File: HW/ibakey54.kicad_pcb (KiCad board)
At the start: 4 copper layers, 164.1 x 143 mm, 106 parts, among them SW1 GATERON-MX-HOTSWAP-RGB, SW10 GATERON-MX-HOTSWAP-RGB, SW11 GATERON-MX-HOTSWAP-RGB, SW12 GATERON-MX-HOTSWAP-RGB, SW13 GATERON-MX-HOTSWAP-RGB, SW14 GATERON-MX-HOTSWAP-RGB, SW15 GATERON-MX-HOTSWAP-RGB, SW16 GATERON-MX-HOTSWAP-RGB, SW17 GATERON-MX-HOTSWAP-RGB, SW18 GATERON-MX-HOTSWAP-RGB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

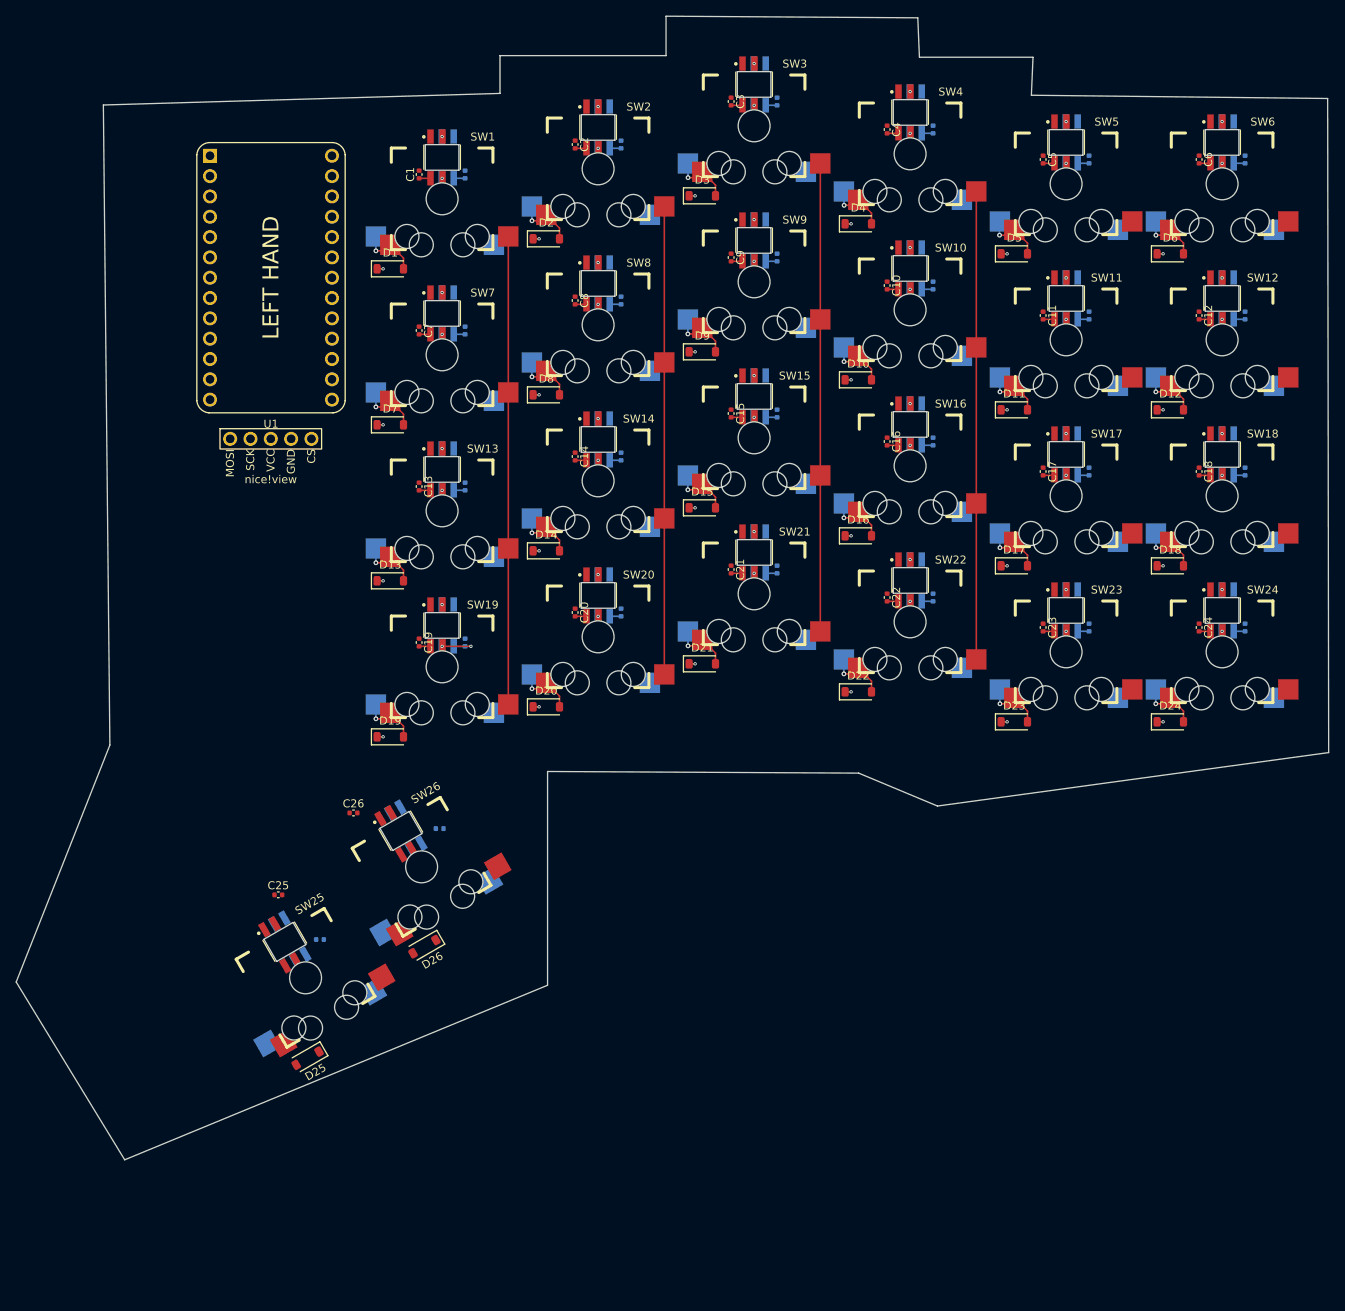
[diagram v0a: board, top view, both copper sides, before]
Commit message: finishing main placement & board shape
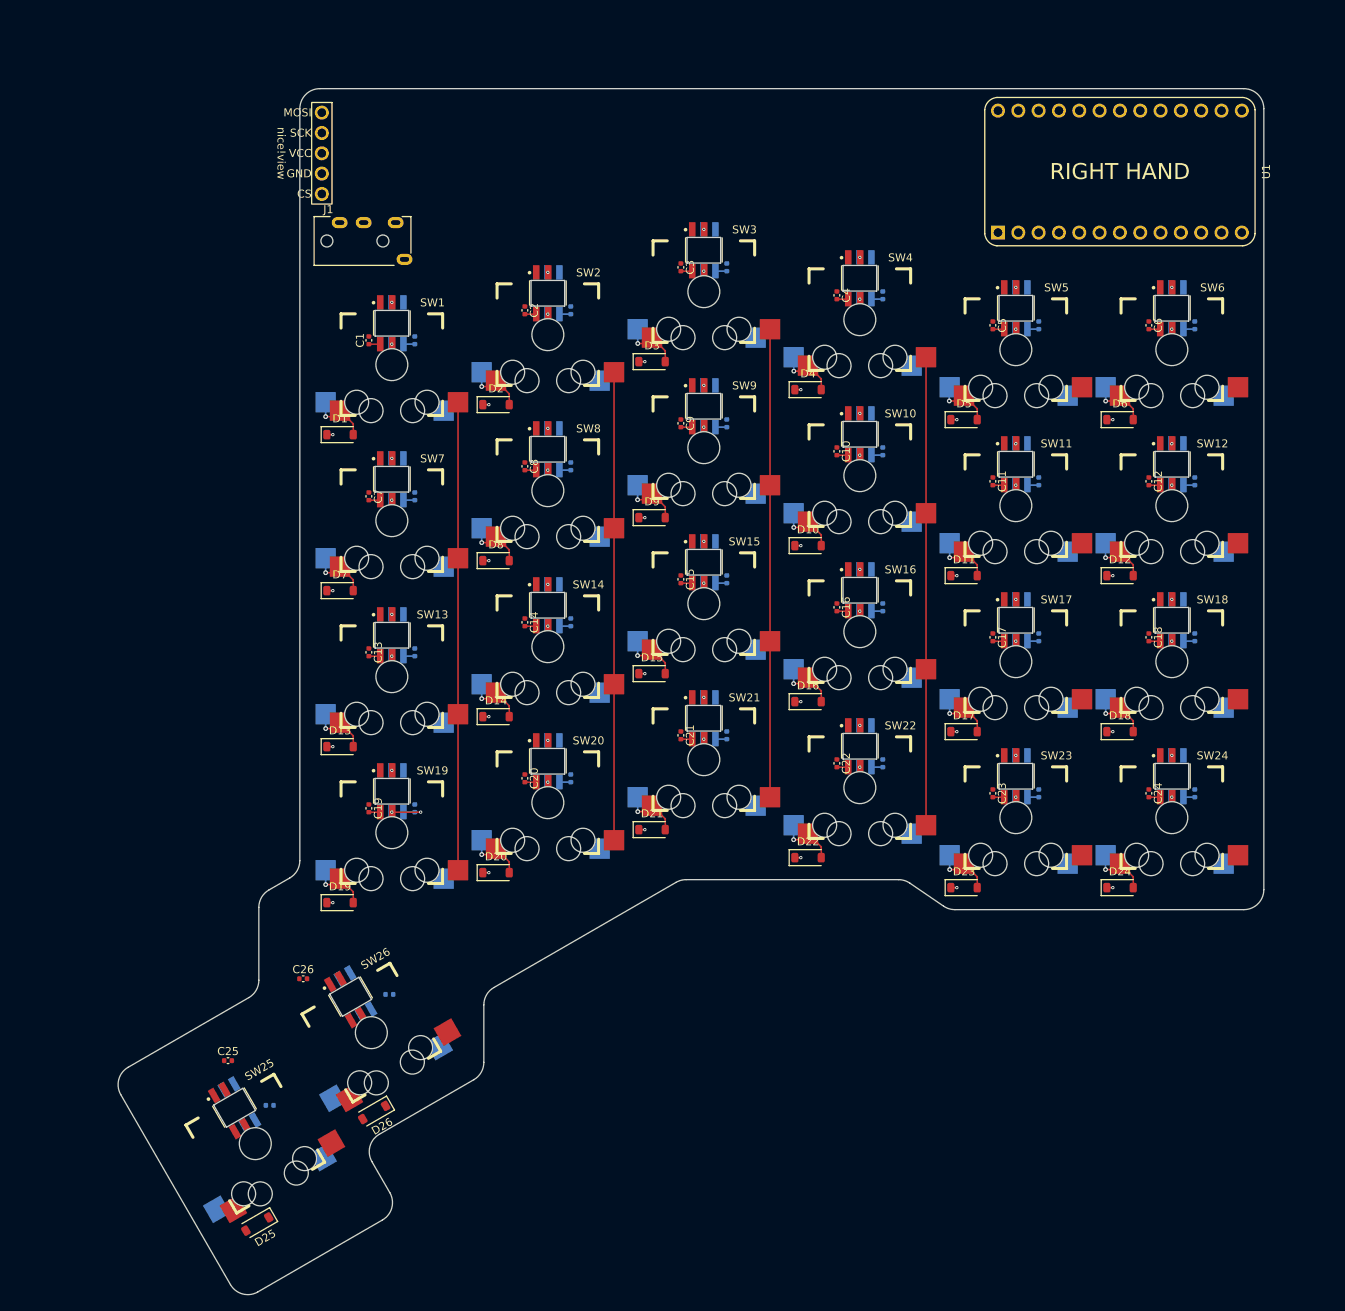
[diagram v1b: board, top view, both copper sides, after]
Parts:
- added J1: AudioJack4, CONN-THT-JACK:PJ-320A, F.Cu at (84.0, 45.3)
- moved U1 106.9 mm to (184.7, 36.6), turned to 90 degrees
- moved Display1 29.9 mm to (101.5, 34.3), turned to -90 degrees
- moved C13 21.7 mm to (90.8, 96.7)
- moved C14 21.7 mm to (110.3, 92.9)
- moved C15 21.7 mm to (129.8, 87.6)
- moved C16 21.7 mm to (149.3, 91.1)
- moved C17 21.7 mm to (168.8, 94.8)
- moved C18 21.7 mm to (188.3, 94.8)
- moved C19 21.7 mm to (90.8, 116.2)
- moved C20 21.7 mm to (110.3, 112.4)
- moved C21 21.7 mm to (129.8, 107.1)
- moved C22 21.7 mm to (149.3, 110.6)
- moved C23 21.7 mm to (168.8, 114.3)
- moved C24 21.7 mm to (188.3, 114.3)
- moved C39 21.7 mm to (96.6, 96.7)
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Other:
- board size 164.1 x 143 mm -> 143.2 x 150.7 mm
